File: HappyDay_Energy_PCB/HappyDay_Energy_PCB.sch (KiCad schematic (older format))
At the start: 34 parts

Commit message: sacrificial draft of power section / HappyDay Energy Monitor Schematic
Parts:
- removed J?: Conn_01x03, symbol Conn_01x03
- removed J?: IP0, symbol TEST_1P
- removed J?: IN0, symbol TEST_1P
- removed J?: IP1, symbol TEST_1P
- removed J?: IN1, symbol TEST_1P
- removed J?: LO_SAMP, symbol TEST_1P
- removed J?: AGND, symbol TEST_1P
- removed J?: +3.3V, symbol TEST_1P
- removed J?: N, symbol TEST_1P
- removed L? (x2): L_Core_Ferrite, symbol L_Core_Ferrite
- removed U?: HLK-PM03, symbol HLK-PM03
- added C? (x2): 1u, symbol C
- added C?: 4.7/400V, symbol CP
- added C?: 150, symbol CP
- added C?: 0.1, symbol C
- added D?: P4KE6.8A, symbol D_TVS
- added J?: Conn_01x04, symbol Conn_01x04
- added U?: TLV1117-33, symbol TLV1117-33
- added U?: VSK-S3-5U, symbol VSK-S3-5U
- C? (x2): value C -> .033u; PN (none) -> C
- R? (x3): PN (none) -> R
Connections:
- net labels added: +5V, 3.3V_AVDD, 5V_UNREG, 5V_UNREG_AC
- net labels removed: +3.3V, +3.3V_ISO, +3.3V_MESSY, AGND, GNDREF, GND_ISO
- wire segments 74 -> 75
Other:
- note added: "120VAC -> +5VDC Unregulated\n"
- note added: "Isolate and Connect AC GND and DC GND\n"
- note added: "Measure and Send"
- note added: "Regulate +3.3V AVDD for use by ATM90E26"
- note added: "Sample Current\n"
- note added: "Sample Voltage\n"
- note removed: "Clean 3.3V\n"
- note removed: "Current Sampling\n"
- note removed: "Measure/Send Readings (DC voltage)"
- note removed: "Voltage Sampling\n"
- moved on the sheet: C?, F?, J?, L?, R?, RV?, U?

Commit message: evolved schematic
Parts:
- added D?: LED, symbol LED
- added R?: 270, symbol R
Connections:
- net +5V: now also R?.1
- net GNDPWR: now also D?.1 (K)
- new net: D?.2 (A), R?.2

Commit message: evolved schematic
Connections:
- net 5V_UNREG_AC renamed 5V_UNREG_A
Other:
- note added: "Isolate Analog and DIgital Signal\n\n"
- note removed: "Isolate and Connect AC GND and DC GND\n"
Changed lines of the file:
@@
-	1    0    0    -1
-$EndComp
-$Comp
-L GNDPWR #PWR?
-U 1 1 5A1214D2
-P 9450 1400
-F 0 "#PWR?" H 9450 1200 50  0001 C CNN
-F 1 "GNDPWR" H 9450 1270 50  0000 C CNN
-F 2 "" H 9450 1350 50  0001 C CNN
-F 3 "" H 9450 1350 50  0001 C CNN
-	1    9450 1400
 	1    0    0    -1
 $EndComp
 Text GLabel 9900 1400 3    60   Output ~ 0
-5V_UNREG_AC
+5V_UNREG_A
 Text GLabel 9600 1400 3    60   Input ~ 0
-5V_UNREG
+5V_UNREG_D
 $Comp
 L ST-PJ-312 J?
@@
 Text GLabel 4700 4150 0    60   Input ~ 0
 GNDA
-$Comp
-L GNDA #PWR?
-U 1 1 5A148A27
-P 4700 2150
-F 0 "#PWR?" H 4700 1900 50  0001 C CNN
-F 1 "GNDA" H 4700 2000 50  0000 C CNN
-F 2 "" H 4700 2150 50  0001 C CNN
-F 3 "" H 4700 2150 50  0001 C CNN
-	1    4700 2150
-	1    0    0    -1
-$EndComp
-$Comp
-L GNDA #PWR?
-U 1 1 5A148ACE
-P 4700 1350
-F 0 "#PWR?" H 4700 1100 50  0001 C CNN
-F 1 "GNDA" H 4700 1200 50  0000 C CNN
-F 2 "" H 4700 1350 50  0001 C CNN
-F 3 "" H 4700 1350 50  0001 C CNN
-	1    4700 1350
-	1    0    0    -1
-$EndComp
 Text GLabel 1400 1800 0    60   Output ~ 0
 GNDA
-$Comp
-L GNDA #PWR?
-U 1 1 5A14B137
-P 9750 1400
-F 0 "#PWR?" H 9750 1150 50  0001 C CNN
-F 1 "GNDA" H 9750 1250 50  0000 C CNN
-F 2 "" H 9750 1400 50  0001 C CNN
-F 3 "" H 9750 1400 50  0001 C CNN
-	1    9750 1400
-	1    0    0    -1
-$EndComp
 Text GLabel 8150 900  2    60   Output ~ 0
-5V_UNREG
+5V_UNREG_D
 $Comp
 L +5V #PWR?
@@
 F 3 "" H 7900 2400 50  0001 C CNN
 	1    7900 2400
-	1    0    0    -1
-$EndComp
-$Comp
-L GNDA #PWR?
-U 1 1 5A14BB1F
-P 7900 2900
-F 0 "#PWR?" H 7900 2650 50  0001 C CNN
-F 1 "GNDA" H 7900 2750 50  0000 C CNN
-F 2 "" H 7900 2900 50  0001 C CNN
-F 3 "" H 7900 2900 50  0001 C CNN
-	1    7900 2900
 	1    0    0    -1
 $EndComp
@@
 Text Notes 6000 650  0    60   ~ 0
 120VAC -> +5VDC Unregulated\n
-Text Notes 8950 650  0    60   ~ 0
-Isolate and Connect AC GND and DC GND\n
+Text Notes 8950 750  0    60   ~ 0
+Isolate Analog and DIgital Signal\n\n
 Text GLabel 7450 2400 0    60   Input ~ 0
-5V_UNREG_AC
+5V_UNREG_A
 Text Notes 8650 2250 0    60   ~ 0
 Regulate +3.3V AVDD for use by ATM90E26
@@
 Connection ~ 7900 1800
 Text GLabel 4700 6000 0    60   Input ~ 0
-5V_UNREG
+5V_UNREG_D
 Text GLabel 7300 1750 0    60   Output ~ 0
-GNDPWR
+GNDD
 Text GLabel 4700 6200 0    60   Input ~ 0
-GNDPWR
+GNDD
+Text GLabel 9450 1400 0    60   Input ~ 0
+GNDD
+Text GLabel 9750 1400 3    60   Output ~ 0
+GNDA
+Text GLabel 7900 2900 0    60   Input ~ 0
+GNDA
+Text GLabel 4700 2150 0    60   Input ~ 0
+GNDA
+Text GLabel 4700 1350 0    60   Input ~ 0
+GNDA
 $EndSCHEMATC

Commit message: evolved schematic
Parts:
- gave numbers to parts that had none: 33
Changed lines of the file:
@@
 L0
 $Comp
-L R R?
+L R R3
 U 1 1 5A10E5D4
 P 2800 800
-F 0 "R?" V 2880 800 50  0000 C CNN
+F 0 "R3" V 2880 800 50  0000 C CNN
 F 1 "R" V 2800 800 50  0000 C CNN
 F 2 "" V 2730 800 50  0001 C CNN
@@
 $EndComp
 $Comp
-L R R?
+L R R5
 U 1 1 5A10E5F6
 P 3250 800
-F 0 "R?" V 3330 800 50  0000 C CNN
+F 0 "R5" V 3330 800 50  0000 C CNN
 F 1 "R" V 3250 800 50  0000 C CNN
 F 2 "" V 3180 800 50  0001 C CNN
@@
 $EndComp
 $Comp
-L R R?
+L R R7
 U 1 1 5A10E61B
 P 3700 800
-F 0 "R?" V 3780 800 50  0000 C CNN
+F 0 "R7" V 3780 800 50  0000 C CNN
 F 1 "R" V 3700 800 50  0000 C CNN
 F 2 "" V 3630 800 50  0001 C CNN
@@
 $EndComp
 $Comp
-L R R?
+L R R9
 U 1 1 5A10E642
 P 4100 800
-F 0 "R?" V 4180 800 50  0000 C CNN
+F 0 "R9" V 4180 800 50  0000 C CNN
 F 1 "R" V 4100 800 50  0000 C CNN
 F 2 "" V 4030 800 50  0001 C CNN
@@
 $EndComp
 $Comp
-L R R?
+L R R11
 U 1 1 5A10E69F
 P 4500 1050
-F 0 "R?" V 4580 1050 50  0000 C CNN
+F 0 "R11" V 4580 1050 50  0000 C CNN
 F 1 "1K" V 4500 1050 50  0000 C CNN
 F 2 "" V 4430 1050 50  0001 C CNN
@@
 $EndComp
 $Comp
-L C C?
+L C C1
 U 1 1 5A119335
 P 4850 1100
-F 0 "C?" H 4875 1200 50  0000 L CNN
+F 0 "C1" H 4875 1200 50  0000 L CNN
 F 1 ".033u" H 4875 1000 50  0000 L CNN
 F 2 "" H 4888 950 50  0001 C CNN
@@
 $EndComp
 $Comp
-L GNDA #PWR?
+L GNDA #PWR01
 U 1 1 5A11BCA0
 P 1400 1900
-F 0 "#PWR?" H 1400 1650 50  0001 C CNN
+F 0 "#PWR01" H 1400 1650 50  0001 C CNN
 F 1 "GNDA" H 1400 1750 50  0000 C CNN
 F 2 "" H 1400 1900 50  0001 C CNN
@@
 $EndComp
 $Comp
-L Varistor RV?
+L Varistor RV1
 U 1 1 5A11BE8A
 P 1200 1350
-F 0 "RV?" V 1325 1350 50  0000 C CNN
+F 0 "RV1" V 1325 1350 50  0000 C CNN
 F 1 "Varistor" V 1075 1350 50  0000 C CNN
 F 2 "" V 1130 1350 50  0001 C CNN
@@
 L1
 $Comp
-L R R?
+L R R4
 U 1 1 5A11C42C
 P 2800 1600
-F 0 "R?" V 2880 1600 50  0000 C CNN
+F 0 "R4" V 2880 1600 50  0000 C CNN
 F 1 "R" V 2800 1600 50  0000 C CNN
 F 2 "" V 2730 1600 50  0001 C CNN
@@
 $EndComp
 $Comp
-L R R?
+L R R6
 U 1 1 5A11C432
 P 3250 1600
-F 0 "R?" V 3330 1600 50  0000 C CNN
+F 0 "R6" V 3330 1600 50  0000 C CNN
 F 1 "R" V 3250 1600 50  0000 C CNN
 F 2 "" V 3180 1600 50  0001 C CNN
@@
 $EndComp
 $Comp
-L R R?
+L R R8
 U 1 1 5A11C438
 P 3700 1600
-F 0 "R?" V 3780 1600 50  0000 C CNN
+F 0 "R8" V 3780 1600 50  0000 C CNN
 F 1 "R" V 3700 1600 50  0000 C CNN
 F 2 "" V 3630 1600 50  0001 C CNN
@@
 $EndComp
 $Comp
-L R R?
+L R R10
 U 1 1 5A11C43E
 P 4100 1600
-F 0 "R?" V 4180 1600 50  0000 C CNN
+F 0 "R10" V 4180 1600 50  0000 C CNN
 F 1 "R" V 4100 1600 50  0000 C CNN
 F 2 "" V 4030 1600 50  0001 C CNN
@@
 $EndComp
 $Comp
-L R R?
+L R R12
 U 1 1 5A11C444
 P 4500 1850
-F 0 "R?" V 4580 1850 50  0000 C CNN
+F 0 "R12" V 4580 1850 50  0000 C CNN
 F 1 "1K" V 4500 1850 50  0000 C CNN
 F 2 "" V 4430 1850 50  0001 C CNN
@@
 $EndComp
 $Comp
-L C C?
+L C C2
 U 1 1 5A11C44A
 P 4850 1900
-F 0 "C?" H 4875 2000 50  0000 L CNN
+F 0 "C2" H 4875 2000 50  0000 L CNN
 F 1 ".033u" H 4875 1800 50  0000 L CNN
 F 2 "" H 4888 1750 50  0001 C CNN
@@
 Sample Voltage\n
 $Comp
-L Ferrite_Bead_Small L?
+L Ferrite_Bead_Small L1
 U 1 1 5A11C7F8
 P 1400 1650
-F 0 "L?" H 1475 1700 50  0000 L CNN
+F 0 "L1" H 1475 1700 50  0000 L CNN
 F 1 "Ferrite_Bead_Small" H 1475 1600 50  0000 L CNN
 F 2 "" V 1330 1650 50  0001 C CNN
@@
 $EndComp
 $Comp
-L Varistor RV?
+L Varistor RV2
 U 1 1 5A11CB55
 P 1600 1350
-F 0 "RV?" V 1725 1350 50  0000 C CNN
+F 0 "RV2" V 1725 1350 50  0000 C CNN
 F 1 "Varistor" V 1475 1350 50  0000 C CNN
 F 2 "" V 1530 1350 50  0001 C CNN
@@
 L0
 $Comp
-L Polyfuse F?
+L Polyfuse F1
 U 1 1 5A120D00
 P 5900 1600
-F 0 "F?" V 5800 1600 50  0000 C CNN
+F 0 "F1" V 5800 1600 50  0000 C CNN
 F 1 "Polyfuse" V 6000 1600 50  0000 C CNN
 F 2 "" H 5950 1400 50  0001 L CNN
@@
 $EndComp
 $Comp
-L GNDPWR #PWR?
+L GNDPWR #PWR02
 U 1 1 5A1212CA
 P 7500 1800
-F 0 "#PWR?" H 7500 1600 50  0001 C CNN
+F 0 "#PWR02" H 7500 1600 50  0001 C CNN
 F 1 "GNDPWR" H 7500 1670 50  0000 C CNN
 F 2 "" H 7500 1750 50  0001 C CNN
@@
 $EndComp
 $Comp
-L dc-dc U?
+L dc-dc U3
 U 1 1 5A1213A4
 P 9300 1050
-F 0 "U?" H 9300 1050 60  0000 C CNN
+F 0 "U3" H 9300 1050 60  0000 C CNN
 F 1 "dc-dc" H 9300 1050 60  0000 C CNN
 F 2 "" H 9300 1050 60  0001 C CNN
@@
 5V_UNREG_D
 $Comp
-L ST-PJ-312 J?
+L ST-PJ-312 J2
 U 1 1 5A123DF5
 P 1350 3350
-F 0 "J?" H 1050 3550 50  0000 C CNN
+F 0 "J2" H 1050 3550 50  0000 C CNN
 F 1 "ST-PJ-312" H 1350 3600 50  0000 C CNN
 F 2 "" H 1400 3310 50  0001 C CNN
@@
 Sample Current\n
 $Comp
-L R R?
+L R R1
 U 1 1 5A12DA2B
 P 2050 3400
-F 0 "R?" V 2130 3400 50  0000 C CNN
+F 0 "R1" V 2130 3400 50  0000 C CNN
 F 1 "12" V 2050 3400 50  0000 C CNN
 F 2 "" V 1980 3400 50  0001 C CNN
@@
 I1P_0
 $Comp
-L ST-PJ-312 J?
+L ST-PJ-312 J3
 U 1 1 5A12DD69
 P 1350 4700
-F 0 "J?" H 1050 4900 50  0000 C CNN
+F 0 "J3" H 1050 4900 50  0000 C CNN
 F 1 "ST-PJ-312" H 1350 4950 50  0000 C CNN
 F 2 "" H 1400 4660 50  0001 C CNN
@@
 $EndComp
 $Comp
-L R R?
+L R R2
 U 1 1 5A12DD6F
 P 2050 4750
-F 0 "R?" V 2130 4750 50  0000 C CNN
+F 0 "R2" V 2130 4750 50  0000 C CNN
 F 1 "12" V 2050 4750 50  0000 C CNN
 F 2 "" V 1980 4750 50  0001 C CNN
@@
 I1N_1
 $Comp
-L TEST_1P J?
+L TEST_1P J4
 U 1 1 5A1334B9
 P 4950 1600
-F 0 "J?" H 4950 1870 50  0000 C CNN
+F 0 "J4" H 4950 1870 50  0000 C CNN
 F 1 "L1_SAMP" H 4950 1800 50  0000 C CNN
 F 2 "" H 5150 1600 50  0001 C CNN
@@
 5V_UNREG_D
 $Comp
-L +5V #PWR?
+L +5V #PWR03
 U 1 1 5A14B98A
 P 8150 900
-F 0 "#PWR?" H 8150 750 50  0001 C CNN
+F 0 "#PWR03" H 8150 750 50  0001 C CNN
 F 1 "+5V" H 8150 1040 50  0000 C CNN
 F 2 "" H 8150 900 50  0001 C CNN
@@
 $EndComp
 $Comp
-L TLV1117-33 U?
+L TLV1117-33 U2
 U 1 1 5A14BA55
 P 7900 2400
-F 0 "U?" H 7750 2525 50  0000 C CNN
+F 0 "U2" H 7750 2525 50  0000 C CNN
 F 1 "TLV1117-33" H 7900 2525 50  0000 L CNN
 F 2 "" H 7900 2400 50  0001 C CNN
@@
 $EndComp
 $Comp
-L C C?
+L C C5
 U 1 1 5A14BF72
 P 7550 2650
-F 0 "C?" H 7575 2750 50  0000 L CNN
+F 0 "C5" H 7575 2750 50  0000 L CNN
 F 1 "1u" H 7575 2550 50  0000 L CNN
 F 2 "" H 7588 2500 50  0001 C CNN
@@
 $EndComp
 $Comp
-L C C?
+L C C7
 U 1 1 5A14C043
 P 8250 2650
-F 0 "C?" H 8275 2750 50  0000 L CNN
+F 0 "C7" H 8275 2750 50  0000 L CNN
 F 1 "1u" H 8275 2550 50  0000 L CNN
 F 2 "" H 8288 2500 50  0001 C CNN
@@
 3.3V_AVDD
 $Comp
-L Conn_01x04 J?
+L Conn_01x04 J1
 U 1 1 5A1573C9
 P 750 1250
-F 0 "J?" H 750 1450 50  0000 C CNN
+F 0 "J1" H 750 1450 50  0000 C CNN
 F 1 "Conn_01x04" H 750 950 50  0000 C CNN
 F 2 "" H 750 1250 50  0001 C CNN
@@
 $EndComp
 $Comp
-L VSK-S3-5U U?
+L VSK-S3-5U U1
 U 1 1 5A1763FC
 P 6700 1050
-F 0 "U?" H 6700 750 60  0000 C CNN
+F 0 "U1" H 6700 750 60  0000 C CNN
 F 1 "VSK-S3-5U" H 6750 1300 60  0000 C CNN
 F 2 "" H 6300 800 60  0001 C CNN
@@
 $EndComp
 $Comp
-L CP C?
+L CP C3
 U 1 1 5A176B2F
 P 5850 1150
-F 0 "C?" H 5875 1250 50  0000 L CNN
+F 0 "C3" H 5875 1250 50  0000 L CNN
 F 1 "4.7/400V" H 5875 1050 50  0000 L CNN
 F 2 "" H 5888 1000 50  0001 C CNN
@@
 $EndComp
 $Comp
-L CP C?
+L CP C4
 U 1 1 5A1778E0
 P 7350 1200
-F 0 "C?" H 7375 1300 50  0000 L CNN
+F 0 "C4" H 7375 1300 50  0000 L CNN
 F 1 "150" H 7375 1100 50  0000 L CNN
 F 2 "" H 7388 1050 50  0001 C CNN
@@
 $EndComp
 $Comp
-L C C?
+L C C6
 U 1 1 5A177AA2
 P 7600 1200
-F 0 "C?" H 7625 1300 50  0000 L CNN
+F 0 "C6" H 7625 1300 50  0000 L CNN
 F 1 "0.1" H 7625 1100 50  0000 L CNN
 F 2 "" H 7638 1050 50  0001 C CNN
@@
 $EndComp
 $Comp
-L D_TVS D?
+L D_TVS D1
 U 1 1 5A177E30
 P 7900 1200
-F 0 "D?" H 7900 1300 50  0000 C CNN
+F 0 "D1" H 7900 1300 50  0000 C CNN
 F 1 "P4KE6.8A" H 7900 1100 50  0000 C CNN
 F 2 "" H 7900 1200 50  0001 C CNN
@@
 F9 "3.3V_AVDD" I L 4700 3950 60
 F10 "GNDA" I L 4700 4150 60
-F11 "GNDPWR" I L 4700 6200 60
-F12 "5V_UNREG" I L 4700 6000 60
+F11 "5V_UNREG_D" I L 4700 6000 60
+F12 "GND_D" I L 4700 6200 60
 $EndSheet
 Text Notes 6000 3750 0    60   ~ 0
 Measure and Send
 $Comp
-L R R?
+L R R13
 U 1 1 5A186D61
 P 8150 1200
-F 0 "R?" V 8230 1200 50  0000 C CNN
+F 0 "R13" V 8230 1200 50  0000 C CNN
 F 1 "270" V 8150 1200 50  0000 C CNN
 F 2 "" V 8080 1200 50  0001 C CNN
@@
 $EndComp
 $Comp
-L LED D?
+L LED D2
 U 1 1 5A186E2C
 P 8150 1600
-F 0 "D?" H 8150 1700 50  0000 C CNN
+F 0 "D2" H 8150 1700 50  0000 C CNN
 F 1 "LED" H 8150 1500 50  0000 C CNN
 F 2 "" H 8150 1600 50  0001 C CNN
@@
 5V_UNREG_D
 Text GLabel 7300 1750 0    60   Output ~ 0
-GNDD
+GND_D
 Text GLabel 4700 6200 0    60   Input ~ 0
-GNDD
+GND_D
 Text GLabel 9450 1400 0    60   Input ~ 0
-GNDD
+GND_D
 Text GLabel 9750 1400 3    60   Output ~ 0
 GNDA

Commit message: evolved layout
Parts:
- removed C3: 4.7/400V, symbol CP
- removed C4: 150, symbol CP
- removed C6: 0.1, symbol C
- removed C7: 1u, symbol C
- removed D1: P4KE6.8A, symbol D_TVS
- removed J1: Conn_01x04, symbol Conn_01x04
- removed J2, J3: ST-PJ-312, symbol ST-PJ-312
- removed J4: L1_SAMP, symbol TEST_1P
- removed U1: VSK-S3-5U, symbol VSK-S3-5U
- removed U2: TLV1117-33, symbol TLV1117-33
- removed U3: dc-dc, symbol dc-dc
- added C3: .001u, Capacitors_SMD:C_0805_HandSoldering, symbol C
- added C4: .1u, Capacitors_SMD:C_0805_HandSoldering, symbol C
- added J1: Conn_01x03, HappyDayEnergyMonitor:3PinConnector, symbol Conn_01x03
- added J2, J3: TRS3.5Female, HappyDayEnergyMonitor:Audio-Jack, symbol TRS3.5Female
- added TP1: 3.3V_A, Connectors_TestPoints:Test_Point_Pad_d2.0mm, symbol TEST
- added TP10: 3.3V_D, Connectors_TestPoints:Test_Point_Pad_d2.0mm, symbol TEST
- added TP11: GND_D, Connectors_TestPoints:Test_Point_Pad_d2.0mm, symbol TEST
- added TP2: GNDA, Connectors_TestPoints:Test_Point_Pad_d2.0mm, symbol TEST
- added TP3: LO_SAMP, Connectors_TestPoints:Test_Point_Pad_d2.0mm, symbol TEST
- added TP4: L1_SAMP, Connectors_TestPoints:Test_Point_Pad_d2.0mm, symbol TEST
- added TP6: I1P_0, Connectors_TestPoints:Test_Point_Pad_d2.0mm, symbol TEST
- added TP7: I1N_0, Connectors_TestPoints:Test_Point_Pad_d2.0mm, symbol TEST
- added TP8: I1P_1, Connectors_TestPoints:Test_Point_Pad_d2.0mm, symbol TEST
- added TP9: I1N_1, Connectors_TestPoints:Test_Point_Pad_d2.0mm, symbol TEST
- added U1: 120VAC->3.3VDC REG, HappyDayEnergyMonitor:RAC03-GA, symbol RAC03-3.3SGA
- added U2: dc-dc, HappyDayEnergyMonitor:DC-DC, symbol dc-dc
- C1, C2: footprint (none) -> Capacitors_SMD:C_0805_HandSoldering
- C5: value 1u -> .001u; footprint (none) -> Capacitors_SMD:C_0805_HandSoldering; PN C -> 202R18W102KV4E
- D2: footprint (none) -> Capacitors_SMD:C_1206_HandSoldering; PN (none) -> IND-LED
- F1: footprint (none) -> HappyDayEnergyMonitor:POLYFUSE; PN (none) -> LVR005NK
- L1: footprint (none) -> Capacitors_SMD:C_1206_HandSoldering; PN (none) -> HI1206T500R-10
- R1, R2: footprint (none) -> Resistors_SMD:R_0805_HandSoldering; PN R -> RL1220S-120-F
- R10, R3, R4, R5, R6, R7, R8, R9: value R -> 220K; footprint (none) -> Resistors_SMD:R_1206_HandSoldering; PN (none) -> R
- R11: footprint (none) -> Resistors_SMD:R_0805_HandSoldering
- R12: footprint (none) -> Resistors_SMD:R_0805_HandSoldering; PN (none) -> R
- R13: value 270 -> 330; footprint (none) -> Resistors_SMD:R_0805_HandSoldering; PN (none) -> R
- RV1, RV2: footprint (none) -> HappyDayEnergyMonitor:MOV; PN (none) -> B72660M0251K072
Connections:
- net 5V_UNREG_A is gone; now on an unnamed net: C5.1
- net GNDPWR is gone; now on an unnamed net: D2.1 (K)
- net GNDA: now also C3.2, TP2.1, U2.3 (OUT-)
- net I1N_0: now also R1.1, J2.1 (sleeve), TP7.1; no longer R1.2
- net I1N_1: now also R2.1, J3.1 (sleeve), TP9.1; no longer R2.2
- net I1P_0: now also R1.2, J2.2 (tip), TP6.1; no longer R1.1
- net I1P_1: now also R2.2, J3.2 (tip), TP8.1; no longer R2.1
- net L0: now also C3.1, C4.1, J1.1 (Pin_1), U1.1 (L)
- net L0_SAMP: now also TP3.1
- net L1: now also J1.2 (Pin_2)
- net L1_SAMP: now also TP4.1
- net N: now also J1.3 (Pin_3)
- net at F1.1: now also C4.2, U1.2 (N)
- net +3V3: now reaches D2.2 (A)
- net +3V3: now also TP10.1, U1.5 (+VO), U2.2 (IN+); no longer R13.2
- net +5V: no longer names the net of R13.1
- new net 3.3V_REG_A: TP1.1, U2.4 (OUT+)
- new net GND_MCU: R13.2, TP11.1, U1.4 (-VO), U2.1 (IN-)
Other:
- note added: "120VAC -> +3.3VDC Regulated\n"
- note added: "Isolate measurement circuit from cpu circuit\n"
- note removed: "120VAC -> +5VDC Unregulated\n"
- note removed: "Isolate Analog and DIgital Signal\n\n"
- note removed: "Regulate +3.3V AVDD for use by ATM90E26"
- moved on the sheet: D2, F1, R13

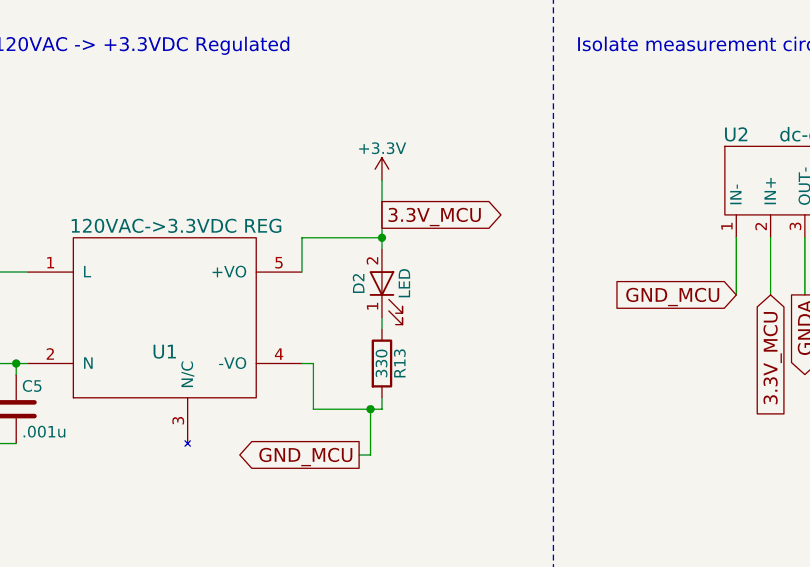
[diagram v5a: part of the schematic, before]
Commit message: files sent to OSH Park for sacrificial draft build
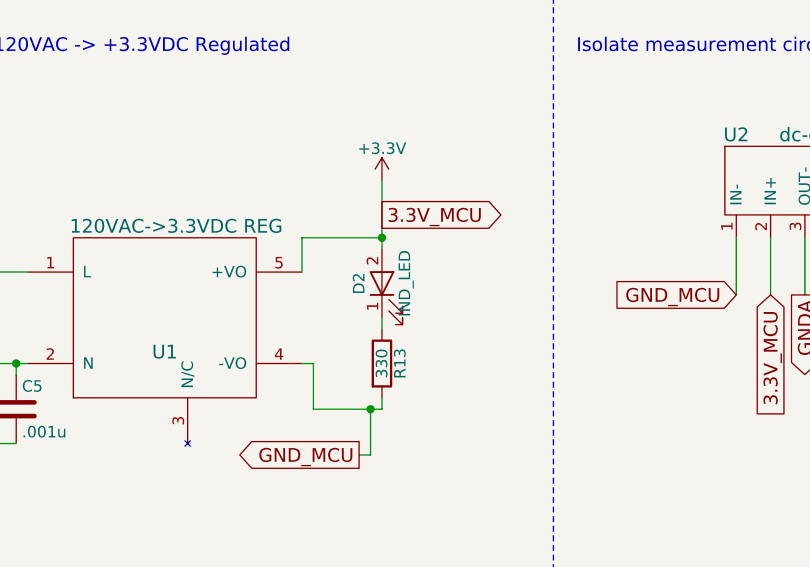
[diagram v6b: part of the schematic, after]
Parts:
- D2: value LED -> IND_LED; PN IND-LED -> LED
- TP1, TP2, TP3: PN (none) -> X
- TP10, TP11, TP4, TP6, TP7, TP8, TP9: PN (none) -> x
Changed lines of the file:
@@
 P 8100 1700
 F 0 "D2" H 8100 1800 50  0000 C CNN
-F 1 "LED" H 8100 1600 50  0000 C CNN
+F 1 "IND_LED" H 8100 1600 50  0000 C CNN
 F 2 "Capacitors_SMD:C_1206_HandSoldering" H 8100 1700 50  0001 C CNN
 F 3 "" H 8100 1700 50  0001 C CNN
-F 4 "IND-LED" H 8100 1700 60  0001 C CNN "PN"
+F 4 "LED" H 8100 1700 60  0001 C CNN "PN"
 	1    8100 1700
 	0    -1   -1   0
@@
 F 2 "Connectors_TestPoints:Test_Point_Pad_d2.0mm" H 5050 3450 50  0001 C CNN
 F 3 "" H 5050 3450 50  0001 C CNN
+F 4 "X" H 5050 3450 60  0001 C CNN "PN"
 	1    5050 3450
 	1    0    0    -1
@@
 F 2 "Connectors_TestPoints:Test_Point_Pad_d2.0mm" H 5050 3900 50  0001 C CNN
 F 3 "" H 5050 3900 50  0001 C CNN
+F 4 "X" H 5050 3900 60  0001 C CNN "PN"
 	1    5050 3900
 	1    0    0    -1
@@
 F 2 "Connectors_TestPoints:Test_Point_Pad_d2.0mm" H 5050 4300 50  0001 C CNN
 F 3 "" H 5050 4300 50  0001 C CNN
+F 4 "X" H 5050 4300 60  0001 C CNN "PN"
 	1    5050 4300
 	1    0    0    -1
@@
 F 2 "Connectors_TestPoints:Test_Point_Pad_d2.0mm" H 5050 4700 50  0001 C CNN
 F 3 "" H 5050 4700 50  0001 C CNN
+F 4 "x" H 5050 4700 60  0001 C CNN "PN"
 	1    5050 4700
 	1    0    0    -1
@@
 F 2 "Connectors_TestPoints:Test_Point_Pad_d2.0mm" H 5050 5500 50  0001 C CNN
 F 3 "" H 5050 5500 50  0001 C CNN
+F 4 "x" H 5050 5500 60  0001 C CNN "PN"
 	1    5050 5500
 	1    0    0    -1
@@
 F 2 "Connectors_TestPoints:Test_Point_Pad_d2.0mm" H 5050 5900 50  0001 C CNN
 F 3 "" H 5050 5900 50  0001 C CNN
+F 4 "x" H 5050 5900 60  0001 C CNN "PN"
 	1    5050 5900
 	1    0    0    -1
@@
 F 2 "Connectors_TestPoints:Test_Point_Pad_d2.0mm" H 5050 6300 50  0001 C CNN
 F 3 "" H 5050 6300 50  0001 C CNN
+F 4 "x" H 5050 6300 60  0001 C CNN "PN"
 	1    5050 6300
 	1    0    0    -1
@@
 F 2 "Connectors_TestPoints:Test_Point_Pad_d2.0mm" H 9350 3550 50  0001 C CNN
 F 3 "" H 9350 3550 50  0001 C CNN
+F 4 "x" H 9350 3550 60  0001 C CNN "PN"
 	1    9350 3550
 	1    0    0    -1
@@
 F 2 "Connectors_TestPoints:Test_Point_Pad_d2.0mm" H 9350 3950 50  0001 C CNN
 F 3 "" H 9350 3950 50  0001 C CNN
+F 4 "x" H 9350 3950 60  0001 C CNN "PN"
 	1    9350 3950
 	1    0    0    -1
@@
 F 2 "Connectors_TestPoints:Test_Point_Pad_d2.0mm" H 9350 4400 50  0001 C CNN
 F 3 "" H 9350 4400 50  0001 C CNN
+F 4 "x" H 9350 4400 60  0001 C CNN "PN"
 	1    9350 4400
 	1    0    0    -1

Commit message: added a css file
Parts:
- R13: value 330 -> 499
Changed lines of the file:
@@
 P 8100 2050
 F 0 "R13" V 8180 2050 50  0000 C CNN
-F 1 "330" V 8100 2050 50  0000 C CNN
+F 1 "499" V 8100 2050 50  0000 C CNN
 F 2 "Resistors_SMD:R_0805_HandSoldering" V 8030 2050 50  0001 C CNN
 F 3 "" H 8100 2050 50  0001 C CNN

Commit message: updates, particularly to layout - but not finished
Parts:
- added C23, C24, C25, C26: .33u, Capacitors_SMD:C_0805, symbol C
- added R25, R26, R27, R28: 100, Capacitors_SMD:C_0805, symbol R
- C1, C2, C3, C4, C5: footprint Capacitors_SMD:C_0805_HandSoldering -> Capacitors_SMD:C_0805
- L1: footprint Capacitors_SMD:C_1206_HandSoldering -> Capacitors_SMD:C_1206
- R1, R11, R12, R13, R2: footprint Resistors_SMD:R_0805_HandSoldering -> Capacitors_SMD:C_0805
- R10, R3, R4, R5, R6, R7, R8, R9: footprint Resistors_SMD:R_1206_HandSoldering -> Capacitors_SMD:C_1206
- U1: value 120VAC->3.3VDC REG -> RAC03-3.3SGA; PN RAC03-3.3SGA -> RAC04-3.3SGB
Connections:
- net GNDA: now also C23.2, C24.1, C25.2, C26.1
- net I1N_0: now also C23.1, R25.1; no longer J2.1 (sleeve), R1.1
- net I1N_1: now also C25.1, R27.1; no longer J3.1 (sleeve), R2.1
- net I1P_0: now also C24.2, R26.1; no longer J2.2 (tip), R1.2
- net I1P_1: now also C26.2, R28.1; no longer J3.2 (tip), R2.2
- new net: J2.1 (sleeve), R1.1, R25.2
- new net: J2.2 (tip), R1.2, R26.2
- new net: J3.1 (sleeve), R2.1, R27.2
- new net: J3.2 (tip), R2.2, R28.2
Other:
- moved on the sheet: TP1, TP10, TP11, TP2, TP3, TP4, TP6, TP7, TP8, TP9
